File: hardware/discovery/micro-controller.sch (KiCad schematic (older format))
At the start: 28 parts, among them U4 STM32F407VG, U8 MOLEX_microSD_47219-2001, X1 CRYSTAL

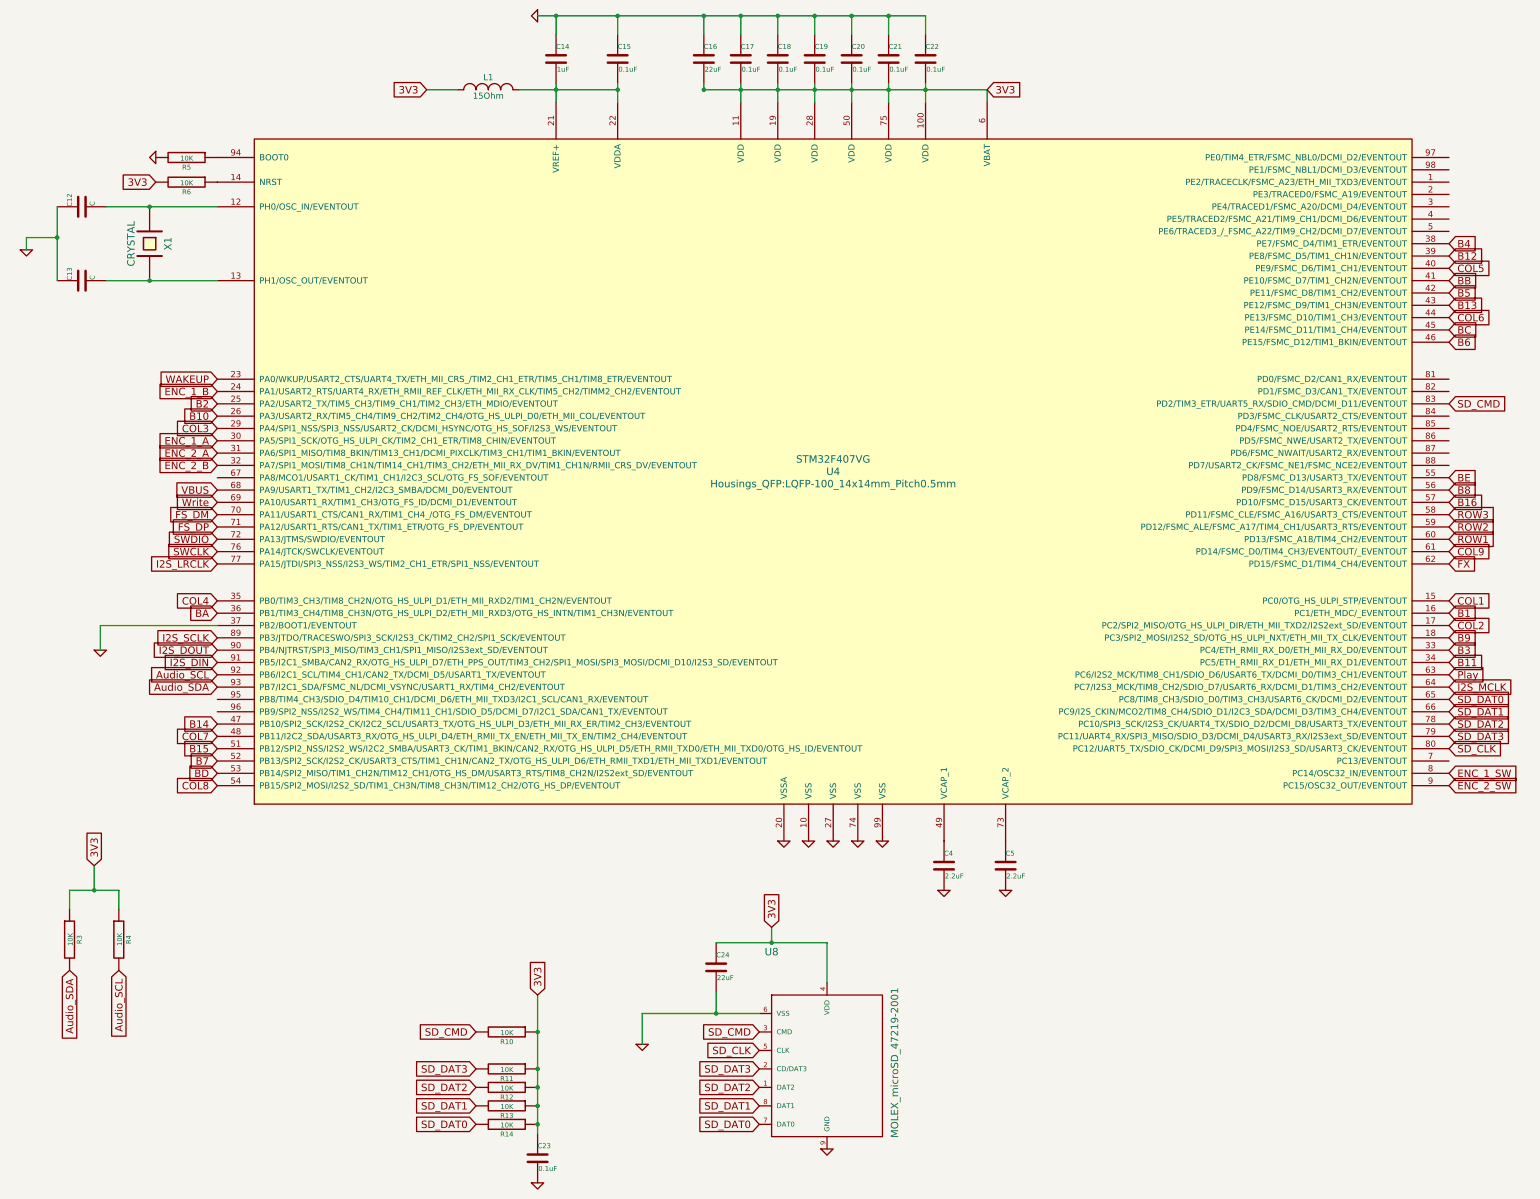
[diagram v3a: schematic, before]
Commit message: Discovery: Add debug port and adjust screen position
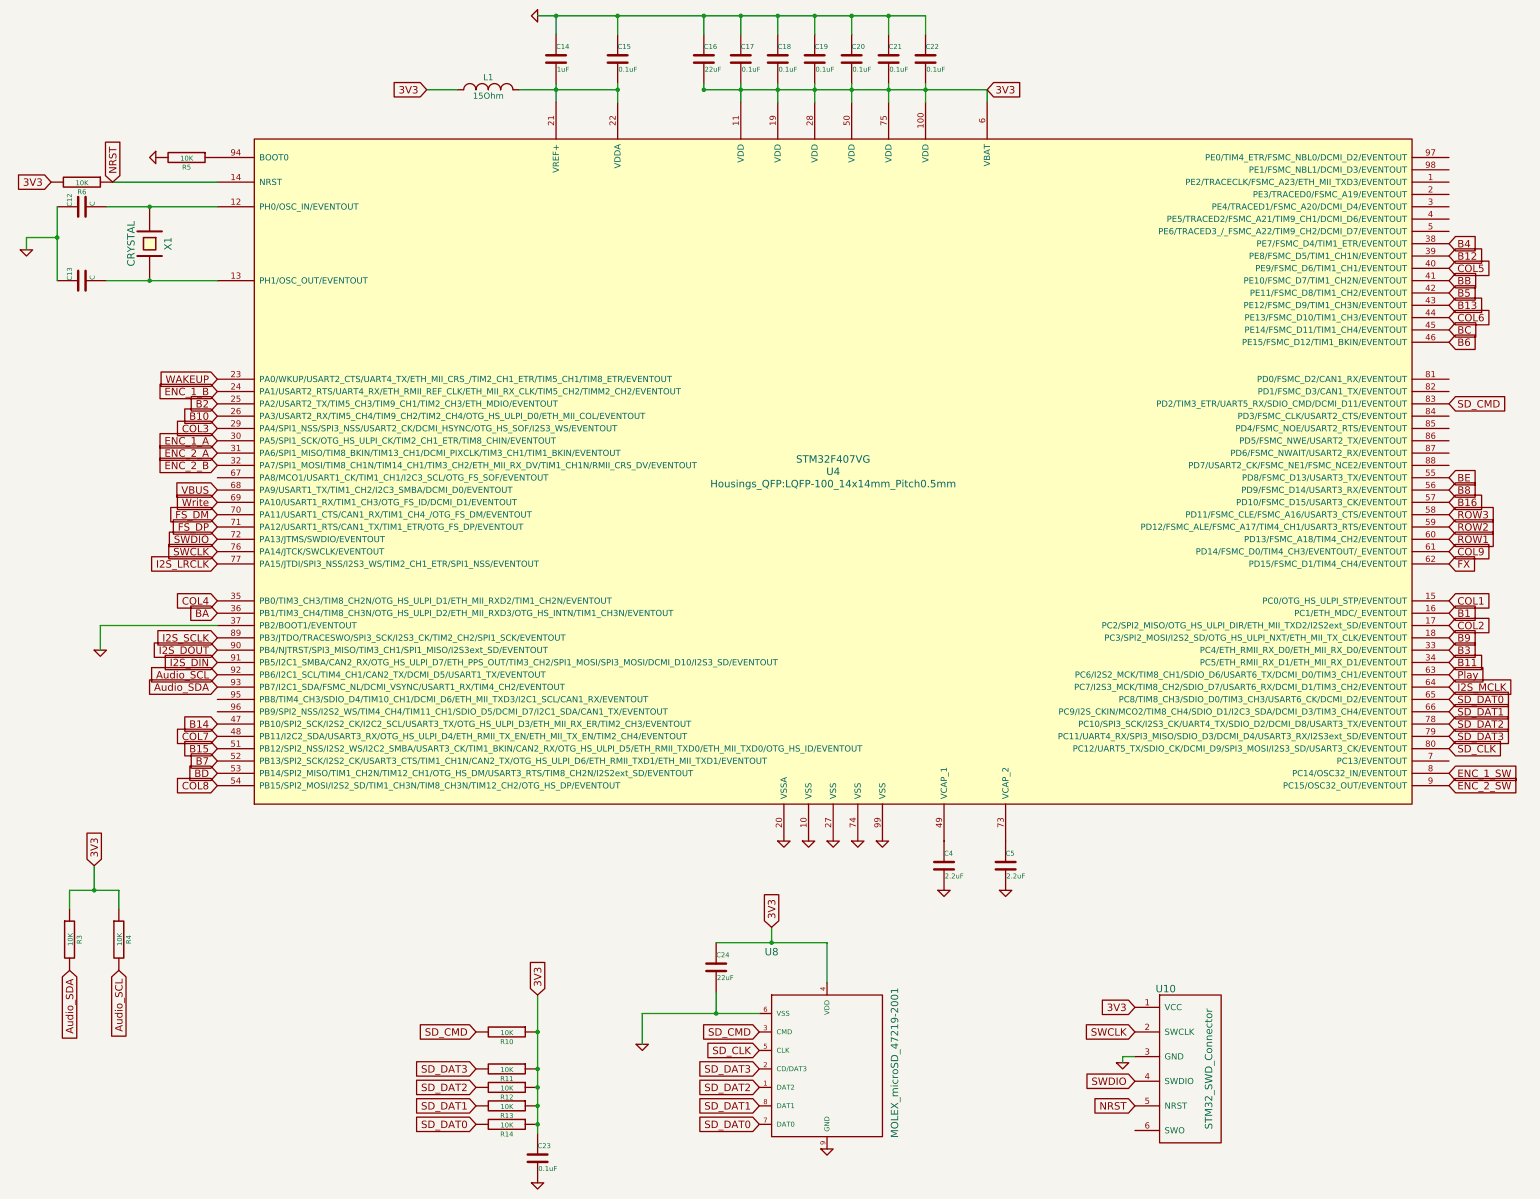
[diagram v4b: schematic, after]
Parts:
- added U10: STM32_SWD_Connector, stm32f4-disco:STM32_SWD_Connector_SMD, symbol STM32_SWD_Connector
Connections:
- net 3V3: now also U10.1 (VCC)
- net GND: now also U10.3 (GND)
- net SWCLK: now also U10.2 (SWCLK)
- net SWDIO: now also U10.4 (SWDIO)
- net NRST: now reaches R6.1, U4.14 (NRST)
- net NRST: now also U10.5 (NRST)
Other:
- moved on the sheet: R6
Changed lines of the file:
@@
 FS_DP
 $Comp
-L GND #PWR21
+L GND #PWR017
 U 1 1 585E3358
 P 7650 7850
-F 0 "#PWR21" H 7650 7850 30  0001 C CNN
+F 0 "#PWR017" H 7650 7850 30  0001 C CNN
 F 1 "GND" H 7650 7780 30  0001 C CNN
 F 2 "" H 7650 7850 60  0001 C CNN
@@
 $EndComp
 $Comp
-L GND #PWR23
+L GND #PWR018
 U 1 1 585E336D
 P 7850 7850
-F 0 "#PWR23" H 7850 7850 30  0001 C CNN
+F 0 "#PWR018" H 7850 7850 30  0001 C CNN
 F 1 "GND" H 7850 7780 30  0001 C CNN
 F 2 "" H 7850 7850 60  0001 C CNN
@@
 $EndComp
 $Comp
-L GND #PWR24
+L GND #PWR019
 U 1 1 585E337B
 P 8050 7850
-F 0 "#PWR24" H 8050 7850 30  0001 C CNN
+F 0 "#PWR019" H 8050 7850 30  0001 C CNN
 F 1 "GND" H 8050 7780 30  0001 C CNN
 F 2 "" H 8050 7850 60  0001 C CNN
@@
 $EndComp
 $Comp
-L GND #PWR25
+L GND #PWR020
 U 1 1 585E3389
 P 8250 7850
-F 0 "#PWR25" H 8250 7850 30  0001 C CNN
+F 0 "#PWR020" H 8250 7850 30  0001 C CNN
 F 1 "GND" H 8250 7780 30  0001 C CNN
 F 2 "" H 8250 7850 60  0001 C CNN
@@
 $EndComp
 $Comp
-L GND #PWR20
+L GND #PWR021
 U 1 1 585E3397
 P 7450 7850
-F 0 "#PWR20" H 7450 7850 30  0001 C CNN
+F 0 "#PWR021" H 7450 7850 30  0001 C CNN
 F 1 "GND" H 7450 7780 30  0001 C CNN
 F 2 "" H 7450 7850 60  0001 C CNN
@@
 $EndComp
 $Comp
-L GND #PWR26
+L GND #PWR022
 U 1 1 585E35DF
 P 8750 8250
-F 0 "#PWR26" H 8750 8250 30  0001 C CNN
+F 0 "#PWR022" H 8750 8250 30  0001 C CNN
 F 1 "GND" H 8750 8180 30  0001 C CNN
 F 2 "" H 8750 8250 60  0001 C CNN
@@
 $EndComp
 $Comp
-L GND #PWR27
+L GND #PWR023
 U 1 1 585E35F3
 P 9250 8250
-F 0 "#PWR27" H 9250 8250 30  0001 C CNN
+F 0 "#PWR023" H 9250 8250 30  0001 C CNN
 F 1 "GND" H 9250 8180 30  0001 C CNN
 F 2 "" H 9250 8250 60  0001 C CNN
@@
 $EndComp
 $Comp
-L GND #PWR14
+L GND #PWR024
 U 1 1 585F8908
 P 1300 3050
-F 0 "#PWR14" H 1300 3050 30  0001 C CNN
+F 0 "#PWR024" H 1300 3050 30  0001 C CNN
 F 1 "GND" H 1300 2980 30  0001 C CNN
 F 2 "" H 1300 3050 60  0001 C CNN
@@
 L R R6
 U 1 1 586123C6
-P 2600 2500
-F 0 "R6" V 2680 2500 40  0000 C CNN
-F 1 "10K" V 2607 2501 40  0000 C CNN
-F 2 "Resistors_SMD:R_0805" V 2530 2500 30  0001 C CNN
-F 3 "" H 2600 2500 30  0000 C CNN
-	1    2600 2500
-	0    1    1    0
-$EndComp
-$Comp
-L GND #PWR16
+P 1750 2500
+F 0 "R6" V 1830 2500 40  0000 C CNN
+F 1 "10K" V 1757 2501 40  0000 C CNN
+F 2 "Resistors_SMD:R_0805" V 1680 2500 30  0001 C CNN
+F 3 "" H 1750 2500 30  0000 C CNN
+	1    1750 2500
+	0    1    1    0
+$EndComp
+$Comp
+L GND #PWR025
 U 1 1 58612418
 P 2350 2300
-F 0 "#PWR16" H 2350 2300 30  0001 C CNN
+F 0 "#PWR025" H 2350 2300 30  0001 C CNN
 F 1 "GND" H 2350 2230 30  0001 C CNN
 F 2 "" H 2350 2300 60  0001 C CNN
@@
 	0    1    1    0
 $EndComp
-Text GLabel 2350 2500 0    60   Input ~ 0
+Text GLabel 1500 2500 0    60   Input ~ 0
 3V3
 $Comp
-L GND #PWR17
+L GND #PWR026
 U 1 1 58612E50
 P 5450 1150
-F 0 "#PWR17" H 5450 1150 30  0001 C CNN
+F 0 "#PWR026" H 5450 1150 30  0001 C CNN
 F 1 "GND" H 5450 1080 30  0001 C CNN
 F 2 "" H 5450 1150 60  0001 C CNN
@@
 $EndComp
 $Comp
-L GND #PWR15
+L GND #PWR027
 U 1 1 5861353A
 P 1900 6300
-F 0 "#PWR15" H 1900 6300 30  0001 C CNN
+F 0 "#PWR027" H 1900 6300 30  0001 C CNN
 F 1 "GND" H 1900 6230 30  0001 C CNN
 F 2 "" H 1900 6300 60  0001 C CNN
@@
 $EndComp
 $Comp
-L GND #PWR22
+L GND #PWR028
 U 1 1 586394FE
 P 7800 10350
-F 0 "#PWR22" H 7800 10350 30  0001 C CNN
+F 0 "#PWR028" H 7800 10350 30  0001 C CNN
 F 1 "GND" H 7800 10280 30  0001 C CNN
 F 2 "" H 7800 10350 60  0001 C CNN
@@
 SD_CMD
 $Comp
-L GND #PWR19
+L GND #PWR029
 U 1 1 58631320
 P 6300 9500
-F 0 "#PWR19" H 6300 9500 30  0001 C CNN
+F 0 "#PWR029" H 6300 9500 30  0001 C CNN
 F 1 "GND" H 6300 9430 30  0001 C CNN
 F 2 "" H 6300 9500 60  0001 C CNN
@@
 $EndComp
 $Comp
-L GND #PWR18
+L GND #PWR030
 U 1 1 58640311
 P 5450 10625
-F 0 "#PWR18" H 5450 10625 30  0001 C CNN
+F 0 "#PWR030" H 5450 10625 30  0001 C CNN
 F 1 "GND" H 5450 10555 30  0001 C CNN
 F 2 "" H 5450 10625 60  0001 C CNN
@@
 Text GLabel 12850 7400 2    60   Input ~ 0
 ENC_2_SW
+$Comp
+L STM32_SWD_Connector U10
+U 1 1 58664887
+P 10550 9050
+F 0 "U10" H 10550 9050 60  0000 C CNN
+F 1 "STM32_SWD_Connector" V 10900 8400 60  0000 C CNN
+F 2 "stm32f4-disco:STM32_SWD_Connector_SMD" H 10550 9050 60  0001 C CNN
+F 3 "" H 10550 9050 60  0001 C CNN
+	1    10550 9050
+	1    0    0    -1
+$EndComp
+Text GLabel 10300 9200 0    60   Input ~ 0
+3V3
+$Comp
+L GND #PWR031
+U 1 1 586649ED
+P 10200 9650
+F 0 "#PWR031" H 10200 9650 30  0001 C CNN
+F 1 "GND" H 10200 9580 30  0001 C CNN
+F 2 "" H 10200 9650 60  0001 C CNN
+F 3 "" H 10200 9650 60  0001 C CNN
+	1    10200 9650
+	1    0    0    -1
+$EndComp
+Wire Wire Line
+	10200 9650 10200 9600
+Wire Wire Line
+	10200 9600 10300 9600
+Text GLabel 10300 9400 0    60   Input ~ 0
+SWCLK
+Text GLabel 10300 9800 0    60   Input ~ 0
+SWDIO
+Wire Wire Line
+	2000 2500 2850 2500
+Text GLabel 2000 2500 1    60   Input ~ 0
+NRST
+Text GLabel 10300 10000 0    60   Input ~ 0
+NRST
 $EndSCHEMATC

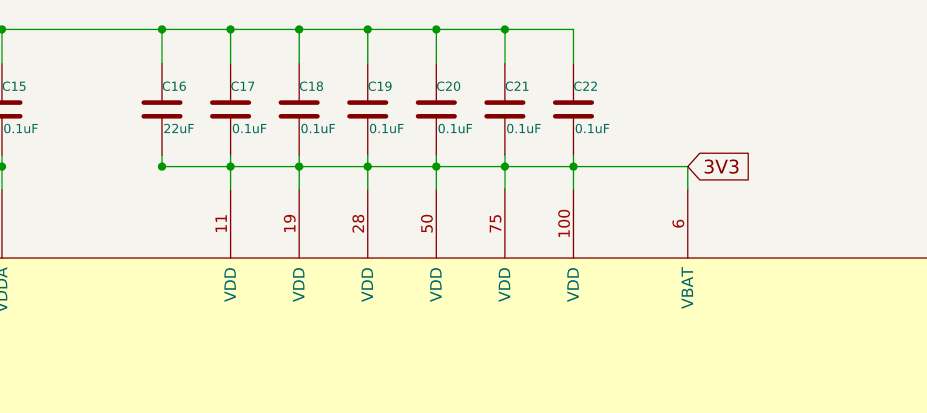
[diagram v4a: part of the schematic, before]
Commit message: Discovery: Connect VBAT to the MCU
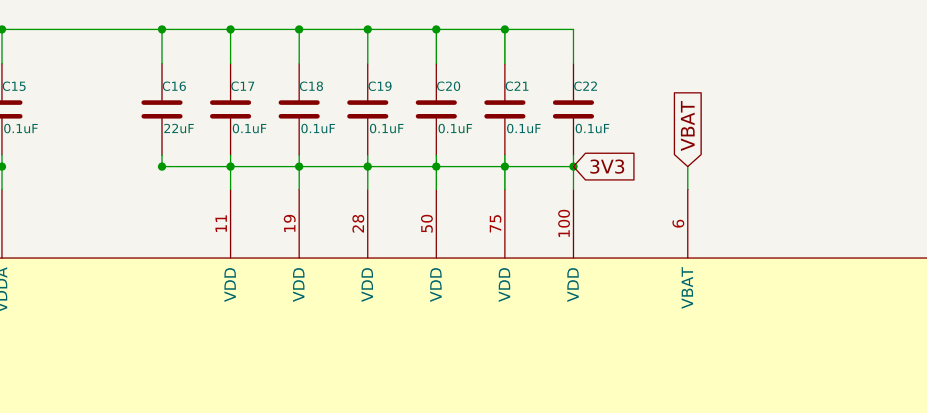
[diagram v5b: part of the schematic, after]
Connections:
- net 3V3: no longer U4.6 (VBAT)
- new net VBAT: U4.6 (VBAT)
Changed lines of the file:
@@
 	1    0    0    -1
 $EndComp
-Text GLabel 9100 1750 2    60   Input ~ 0
+Text GLabel 8600 1750 2    60   Input ~ 0
 3V3
 $Comp
@@
 Connection ~ 8300 1150
 Wire Wire Line
-	9100 1750 6800 1750
-Wire Wire Line
 	5450 1150 8600 1150
 Wire Wire Line
@@
 Text GLabel 10300 10000 0    60   Input ~ 0
 NRST
+Wire Wire Line
+	6800 1750 8600 1750
+Text GLabel 9100 1750 1    60   Input ~ 0
+VBAT
 $EndSCHEMATC
